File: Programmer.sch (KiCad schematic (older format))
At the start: 74 parts, among them CON1 USB_OTG, M1 ESP-12E, P1 CONN_01X12, P3 CONN_12, Q1 BSS138L, Q2 MMBT3906, Q3 MMBT3904, Q4 BSS84, Q5 BSS138L, Q6 MMBT3906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

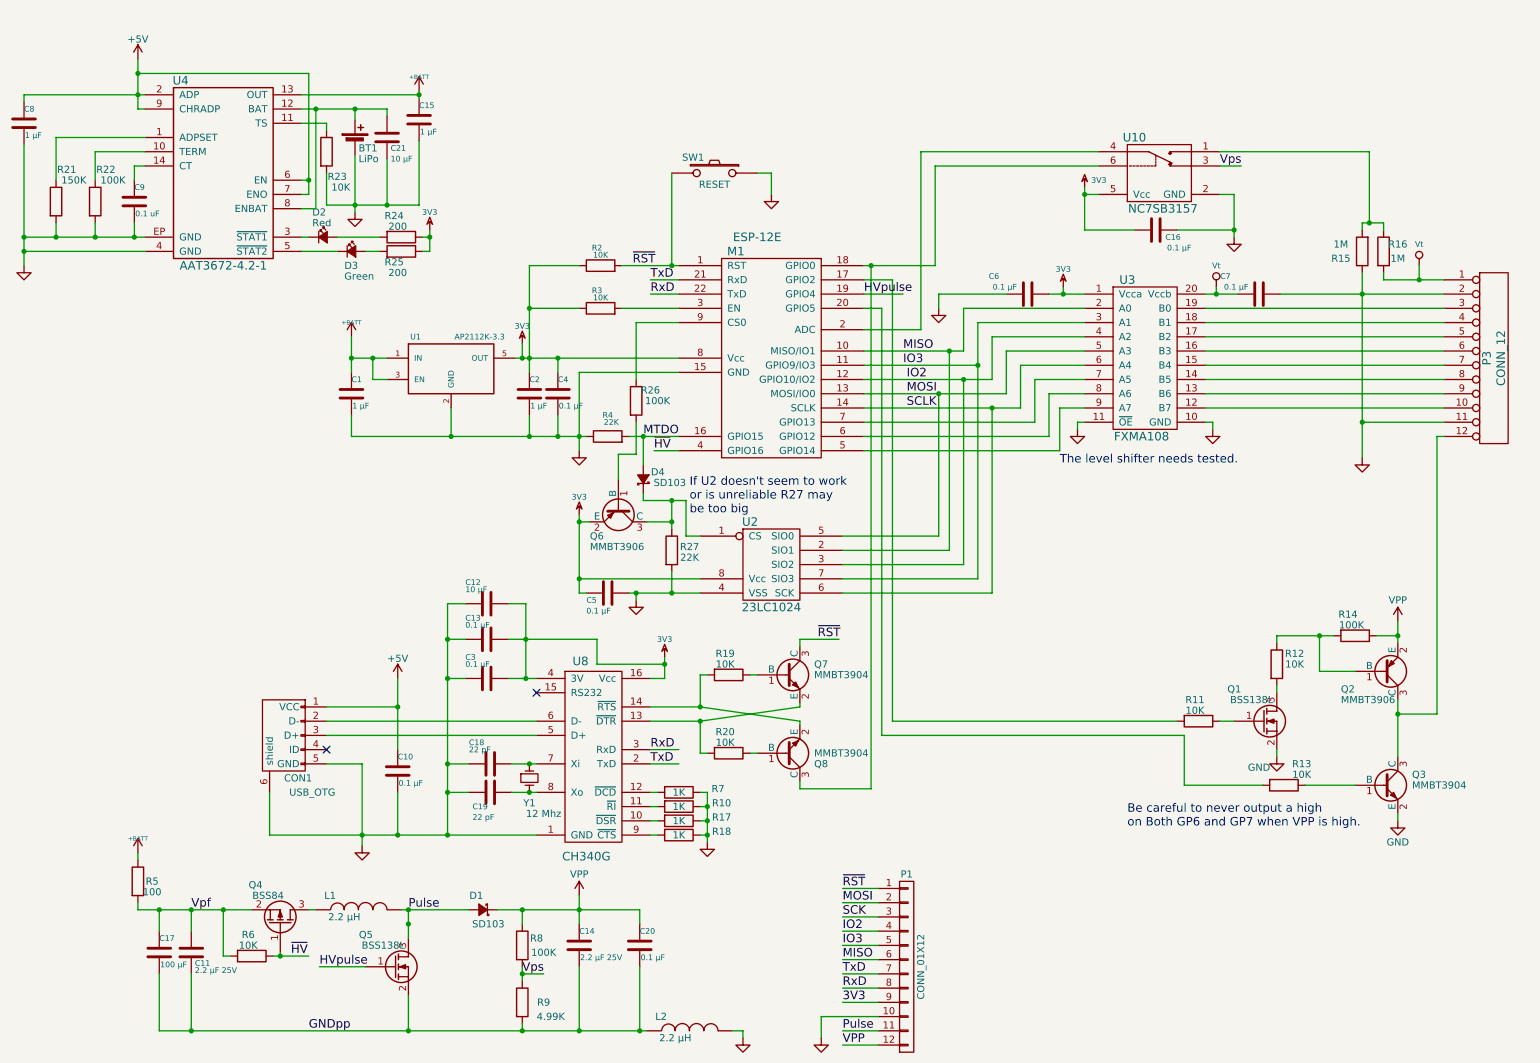
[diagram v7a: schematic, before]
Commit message: Hardware Version 00H
Schematic updated to get ready for a new layout.
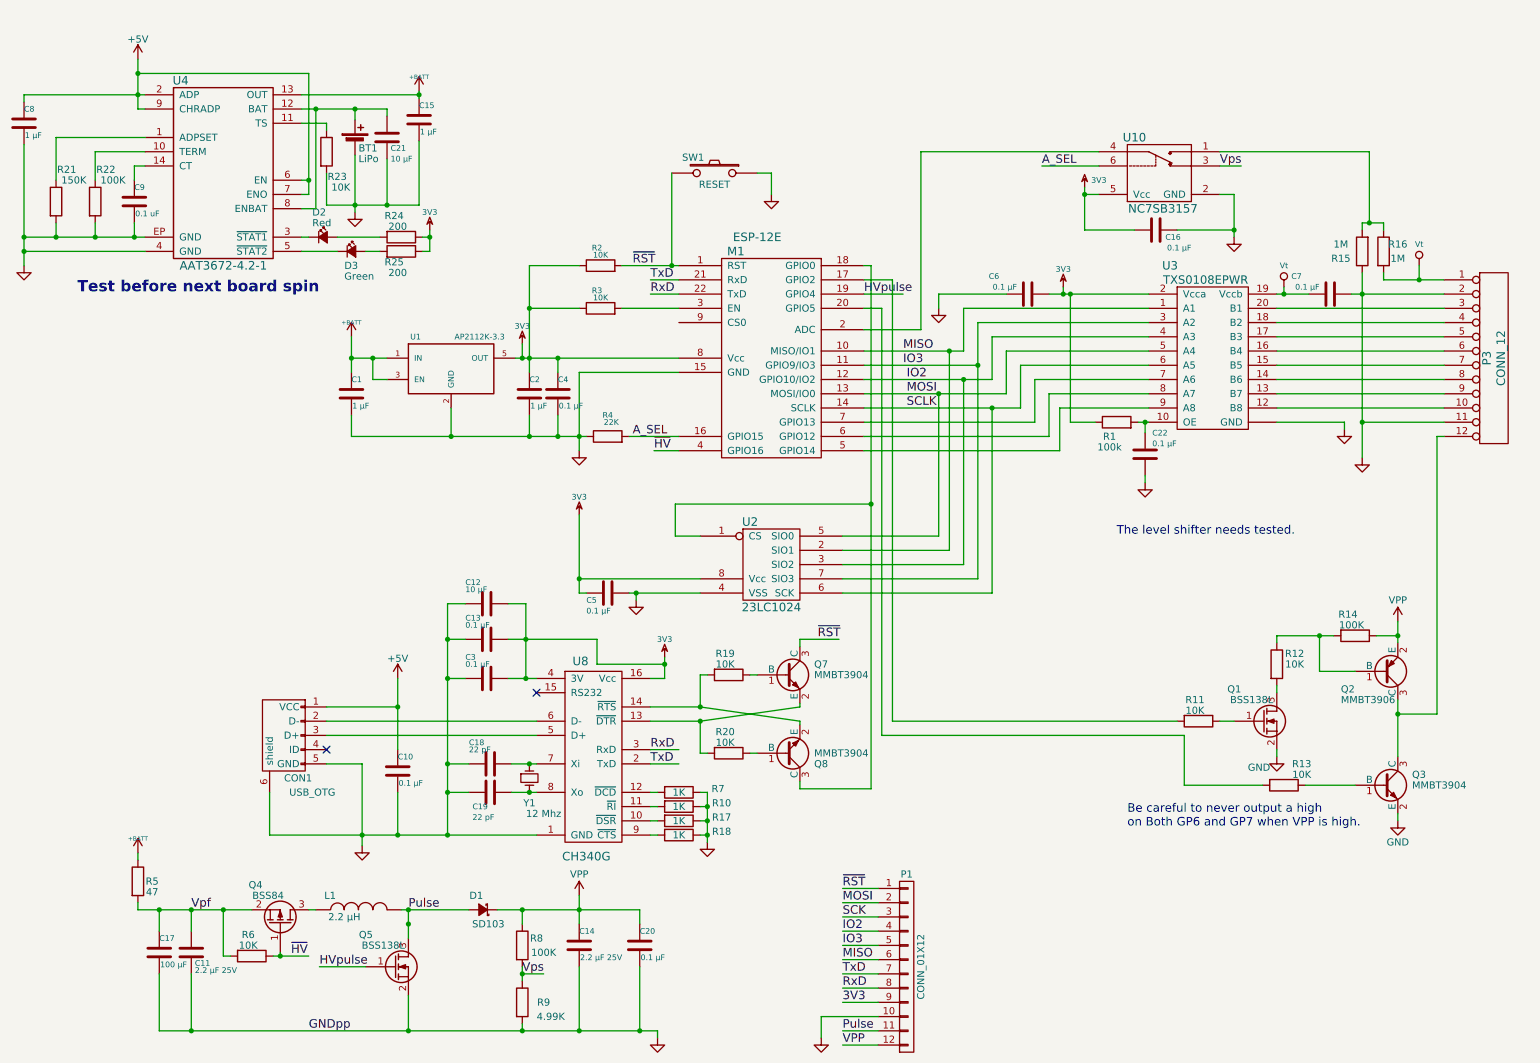
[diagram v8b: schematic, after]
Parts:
- removed D4: SD103, Diodes_SMD:SOD-323, symbol D_Schottky_Small
- removed L2: 2.2 µH, Choke_SMD:Choke_SMD_1206_Standard, symbol INDUCTOR
- removed Q6: MMBT3906, TO_SOT_Packages_SMD:SOT-23, symbol MMBT3906
- removed R26: 100K, Resistors_SMD:R_1206, symbol R
- removed R27: 22K, Resistors_SMD:R_1206, symbol R
- removed U3: FXMA108, Uprogrammer FPs:DQFN20, symbol FXMA108
- added C22: 0.1 µF, Capacitors_SMD:C_1206, symbol C
- added R1: 100k, Resistors_SMD:R_1206, symbol R
- added U3: TXS0108EPWR, Housings_SSOP:TSSOP-20_4.4x6.5mm_Pitch0.65mm, symbol TXB0108PWR
- R5: value 100 -> 47
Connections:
- net GNDpp is gone; now on net GND: C11.2, C14.2, C17.2, C20.2, Q5.2 (S), R9.2
- net 3V3: now also R1.1, U3.2 (Vcca)
- net GND: now also C22.2, U3.~ (GND)
- net IO2: now also U3.4 (A3)
- net IO3: now also U3.3 (A2)
- net MISO: now also U3.1 (A1)
- net MOSI: now also U3.5 (A4)
- net SCLK: now also U3.6 (A5)
- net VEE: now also U3.19 (Vccb)
- net at M1.18 (GPIO0), Q8.3 (C): now also U2.1 (CS); no longer U10.6
- net at M1.5 (GPIO14): now also U3.9 (A8)
- net at M1.6 (GPIO12): now also U3.8 (A7)
- net at M1.7 (GPIO13): now also U3.7 (A6)
- net at P3.10 (P10): now also U3.12 (B8)
- net at P3.3 (P3): now also U3.20 (B1)
- net at P3.4 (P4): now also U3.18 (B2)
- net at P3.5 (P5): now also U3.17 (B3)
- net at P3.6 (P6): now also U3.16 (B4)
- net at P3.7 (P7): now also U3.15 (B5)
- net at P3.8 (P8): now also U3.14 (B6)
- net at P3.9 (P9): now also U3.13 (B7)
- net MTDO renamed A_SEL
- net A_SEL: now also U10.6
- new net: C22.1, R1.2, U3.10 (OE)
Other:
- note added: "Test before next board spin"
- note removed: "If U2 doesn't seem to work \nor is unreliable R27 may \nbe too big"
- moved on the sheet: C7
